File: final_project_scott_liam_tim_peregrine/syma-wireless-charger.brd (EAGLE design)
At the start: 100 x 80 mm, 46 parts, among them U1 SAMD21E

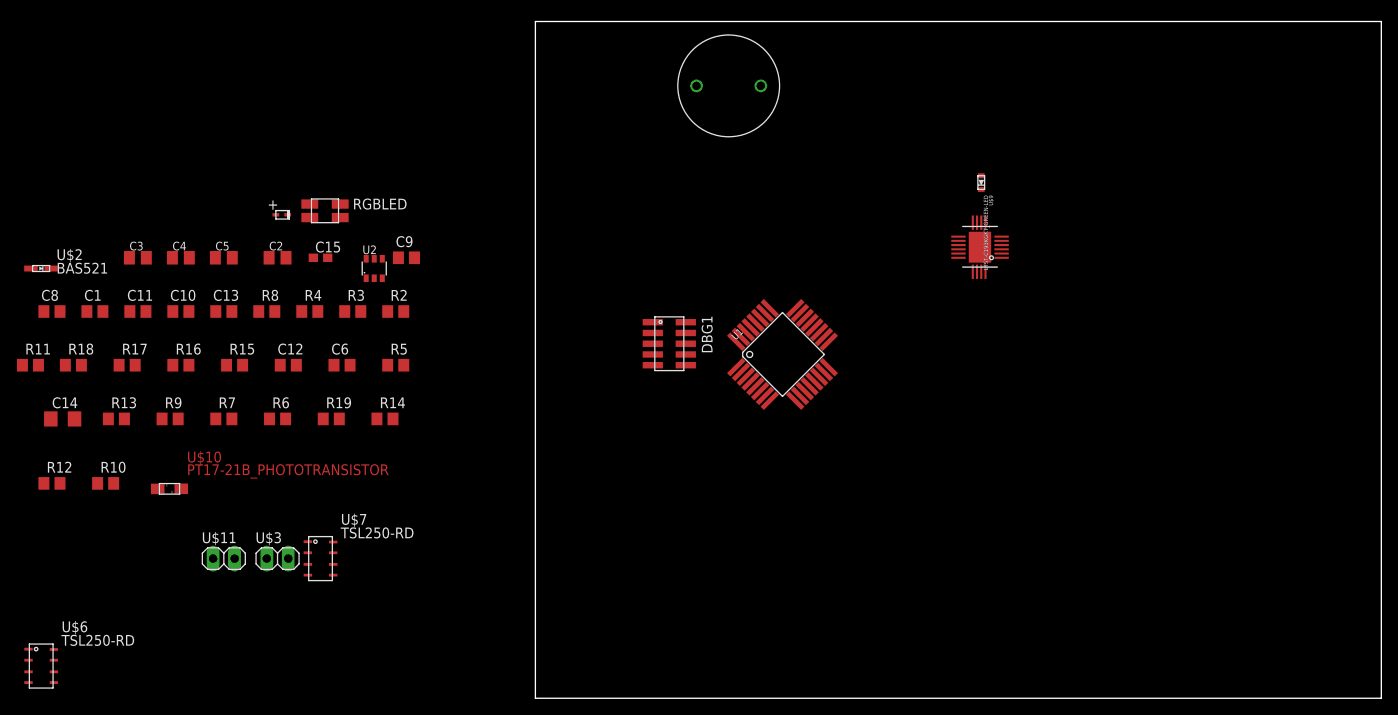
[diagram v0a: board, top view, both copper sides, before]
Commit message: placed parts for transmitter board. no traces yet
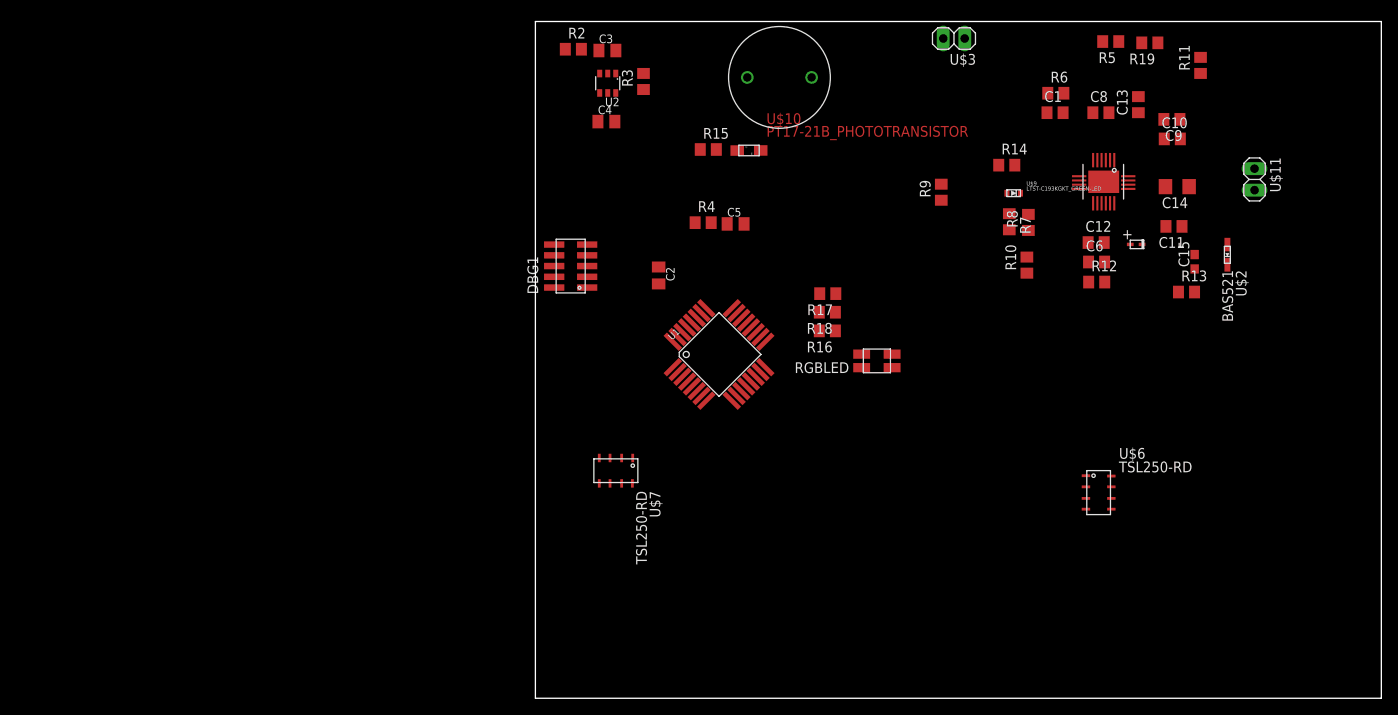
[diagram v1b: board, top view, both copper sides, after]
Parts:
- moved R11 142.8 mm to (78.6, 74.8), turned to 90 degrees
- moved U$2 140.2 mm to (81.8, 52.4), turned to 270 degrees
- moved C14 134.6 mm to (75.9, 60.5), turned to 180 degrees
- moved U$11 129.8 mm to (85.0, 61.3), turned to 270 degrees
- moved R13 127.4 mm to (77.0, 48.0)
- moved U$6 126.7 mm to (66.6, 24.3)
- moved C8 126.2 mm to (66.8, 69.2)
- moved R12 125.8 mm to (66.3, 49.2)
- moved C11 122.9 mm to (75.5, 55.8), turned to 180 degrees
- moved C10 119.0 mm to (75.3, 66.1)
- moved C1 115.9 mm to (61.4, 69.2)
- moved R10 111.9 mm to (58.1, 51.2), turned to 90 degrees
- moved C13 110.8 mm to (71.3, 70.2), turned to 90 degrees
- moved R19 106.5 mm to (72.6, 77.5), turned to 180 degrees
- moved C15 103.3 mm to (77.9, 51.6), turned to 90 degrees
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
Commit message: mostly finished traces
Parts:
- moved U$3 41.5 mm to (8.02, 75.5), turned to 0 degrees
- moved R2 12.6 mm to (5.99, 64.2)
- moved U$7 12.0 mm to (21.5, 26.1), turned to 90 degrees
- moved C4 9.34 mm to (10.9, 59.2)
- moved C8 8.67 mm to (71.8, 76.3), turned to 90 degrees
- moved R3 8.54 mm to (15.8, 64.9)
- moved U2 8.25 mm to (10.6, 64.7)
- moved C3 7.76 mm to (10.5, 69.1)
- moved DBG1 7.63 mm to (8.78, 52.5), turned to 270 degrees
- moved C2 7.16 mm to (17.6, 56.5)
- moved U$5 6.67 mm to (31.6, 71.9)
- moved R9 6.52 mm to (53.5, 56.3)
- moved R19 6.04 mm to (67.1, 75.0)
- moved U$6 5.56 mm to (63.9, 29.2), turned to 180 degrees
- moved U$4 5.00 mm to (45.2, 43.1)
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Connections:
- net GND: now also U$1.GND2
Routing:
- net +5V: track 0.00 -> 156.2 mm, vias 0 -> 4
- net N$20: track 0.00 -> 137.0 mm, vias 0 -> 6
- net VDD: track 0.00 -> 112.2 mm, vias 0 -> 4
- net GND: track 0.00 -> 106.9 mm, vias 0 -> 16
- net ALIGNED: track 0.00 -> 69.0 mm
- net PA17: track 0.00 -> 62.3 mm, vias 0 -> 4
- net RST: track 0.00 -> 46.9 mm
- net N$19: track 0.00 -> 33.5 mm
- net N$7: track 0.00 -> 31.7 mm
- net N$4: track 0.00 -> 26.4 mm, vias 0 -> 2
- net N$9: track 0.00 -> 24.9 mm, vias 0 -> 4
- net ENVSENSE: track 0.00 -> 18.8 mm
- net N$21: track 0.00 -> 15.7 mm
- net SWDCLK-PA30: track 0.00 -> 14.8 mm
- net SWDIO-PA31: track 0.00 -> 14.3 mm, vias 0 -> 2
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- added copper zone on layer 16, net GND
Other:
- board size 100 x 80 mm -> 90.5 x 64.5 mm

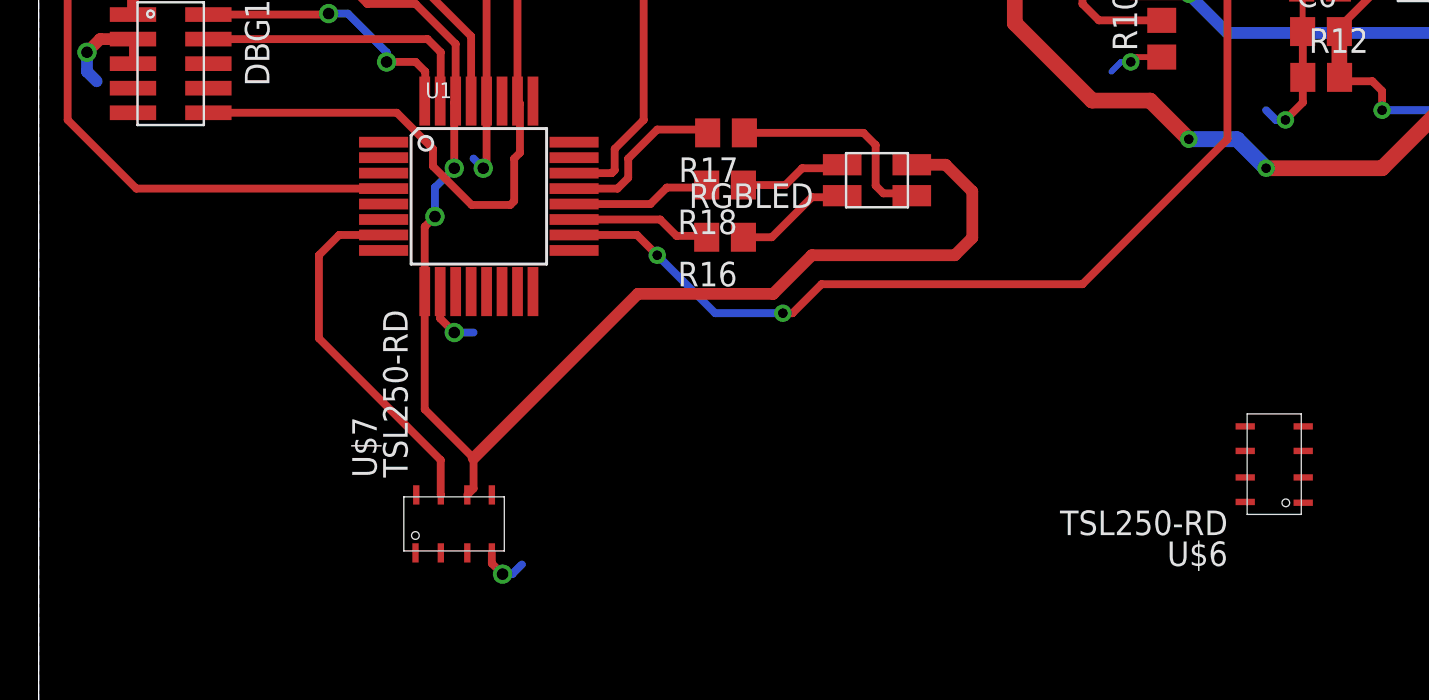
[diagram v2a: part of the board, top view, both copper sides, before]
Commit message: moved the light detectors to be farther from each other
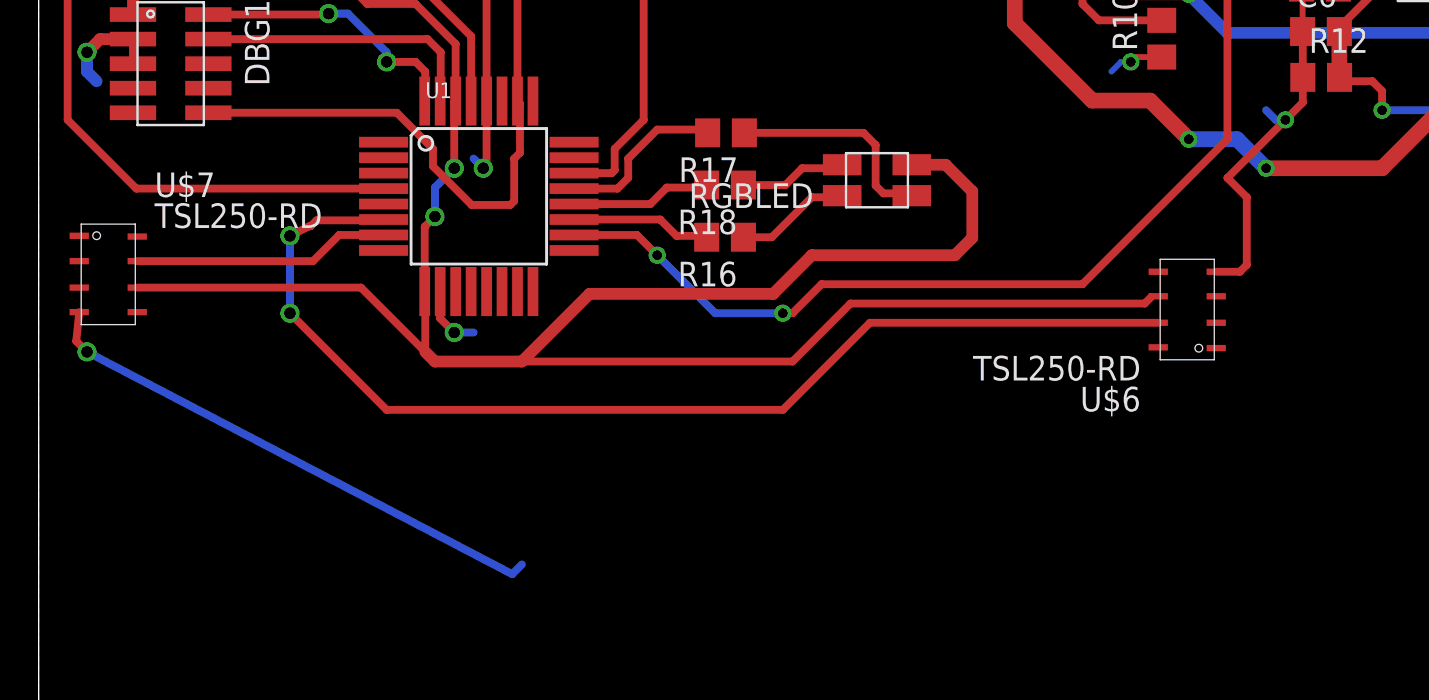
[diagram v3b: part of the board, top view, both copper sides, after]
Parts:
- moved U$7 22.1 mm to (3.60, 39.0), turned to 0 degrees
- moved U$6 9.18 mm to (59.4, 37.2)
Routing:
- net CARSENSE: track 0.00 -> 58.0 mm, vias 0 -> 2
- net VDD: track 112.2 -> 157.8 mm
- net GND: track 106.9 -> 143.0 mm
- net ENVSENSE: track 18.8 -> 13.3 mm
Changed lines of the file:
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@@
 <?xml version="1.0" encoding="utf-8"?>
 <!DOCTYPE eagle SYSTEM "eagle.dtd">
-<eagle version="7.4.0">
+<eagle version="7.5.0">
 <drawing>
 <settings>
@@
 <element name="U$4" library="foe-scale" package="RGBLED" value="RGBLED" x="45.17" y="43.08" rot="R180"/>
 <element name="U$5" library="foe-scale" package="BUZZER" value="BUZZER" x="31.55" y="71.89" rot="R270"/>
-<element name="U$6" library="foe-scale" package="TSL250-RD" value="TSL250-RD" x="63.92" y="29.19" rot="R180"/>
-<element name="U$7" library="foe-scale" package="TSL250-RD" value="TSL250-RD" x="21.49" y="26.1" rot="R90"/>
+<element name="U$6" library="foe-scale" package="TSL250-RD" value="TSL250-RD" x="59.42" y="37.19" rot="R180"/>
+<element name="U$7" library="foe-scale" package="TSL250-RD" value="TSL250-RD" x="3.6" y="39.01"/>
 <element name="U$8" library="foe-scale" package="SOD-523" value="SCHTKYDIODE-523" x="70.52" y="53.65"/>
 <element name="U$9" library="foe-scale" package="LTST-C193KGKT_GREEN-LED" value="LTST-C193KGKT_GREEN-LED" x="56.54" y="59.705"/>
@@
 <via x="21.5" y="36" extent="1-16" drill="0.6"/>
 <wire x1="21.5" y1="36" x2="22.5" y2="36" width="0.4064" layer="16"/>
-<wire x1="23.445" y1="24.6" x2="23.445" y2="24.055" width="0.4064" layer="1"/>
-<wire x1="23.445" y1="24.055" x2="24" y2="23.5" width="0.4064" layer="1"/>
-<via x="24" y="23.5" extent="1-16" drill="0.6"/>
-<wire x1="24" y1="23.5" x2="24.5" y2="23.5" width="0.4064" layer="16"/>
+<wire x1="2.1" y1="37.055" x2="1.945" y2="35.555" width="0.4064" layer="1"/>
+<wire x1="1.945" y1="35.555" x2="2.5" y2="35" width="0.4064" layer="1"/>
+<via x="2.5" y="35" extent="1-16" drill="0.6"/>
+<wire x1="2.5" y1="35" x2="24.5" y2="23.5" width="0.4064" layer="16"/>
 <wire x1="24.5" y1="23.5" x2="25" y2="24" width="0.4064" layer="16"/>
 <wire x1="31.5" y1="71.84" x2="31.55" y2="71.89" width="0.4064" layer="1"/>
@@
 <via x="76" y="51.5" extent="1-16" drill="0.5"/>
 <wire x1="76" y1="51.5" x2="75.5" y2="51" width="0.6096" layer="16"/>
-<wire x1="64.5" y1="47" x2="65.42" y2="31.145" width="0" layer="19" extent="1-1"/>
+<wire x1="60.92" y1="39.145" x2="62.145" y2="39.145" width="0.4064" layer="1"/>
+<wire x1="62.145" y1="39.145" x2="62.5" y2="39.5" width="0.4064" layer="1"/>
+<wire x1="62.5" y1="39.5" x2="62.5" y2="43" width="0.4064" layer="1"/>
+<wire x1="62.5" y1="43" x2="61.5" y2="44" width="0.4064" layer="1"/>
+<wire x1="61.5" y1="44" x2="64.5" y2="47" width="0.4064" layer="1"/>
 </signal>
 <signal name="N$3">
@@
 <wire x1="21.5" y1="44.5" x2="21.5" y2="47.90168125" width="0.4064" layer="1"/>
 <wire x1="21.5" y1="47.90168125" x2="21.572615625" y2="47.974296875" width="0.4064" layer="1"/>
-<wire x1="19.972615625" y1="38.119096875" x2="19.972615625" y2="32.027384375" width="0.4064" layer="1"/>
-<wire x1="19.972615625" y1="32.027384375" x2="22.5" y2="29.5" width="0.4064" layer="1"/>
-<wire x1="22.5" y1="29.5" x2="22.5" y2="27.925" width="0.4064" layer="1"/>
-<wire x1="22.5" y1="27.925" x2="22.175" y2="27.6" width="0.4064" layer="1"/>
 <wire x1="45.17" y1="44.68" x2="46.92" y2="44.68" width="0.6096" layer="1"/>
 <wire x1="46.92" y1="44.68" x2="48.3" y2="43.3" width="0.6096" layer="1"/>
@@
 <wire x1="47.4" y1="40" x2="40" y2="40" width="0.6096" layer="1"/>
 <wire x1="40" y1="40" x2="38" y2="38" width="0.6096" layer="1"/>
-<wire x1="38" y1="38" x2="31" y2="38" width="0.6096" layer="1"/>
-<wire x1="31" y1="38" x2="22.5" y2="29.5" width="0.6096" layer="1"/>
+<wire x1="38" y1="38" x2="28.5" y2="38" width="0.6096" layer="1"/>
+<wire x1="5.1" y1="38.325" x2="16.675" y2="38.325" width="0.4064" layer="1"/>
+<wire x1="16.675" y1="38.325" x2="20" y2="35" width="0.4064" layer="1"/>
+<wire x1="28.5" y1="38" x2="25" y2="34.5" width="0.6096" layer="1"/>
+<wire x1="25" y1="34.5" x2="20.5" y2="34.5" width="0.6096" layer="1"/>
+<wire x1="20.5" y1="34.5" x2="20" y2="35" width="0.6096" layer="1"/>
+<wire x1="20" y1="37" x2="20" y2="35" width="0.4064" layer="1"/>
+<wire x1="20.5" y1="34.5" x2="39" y2="34.5" width="0.4064" layer="1"/>
+<wire x1="39" y1="34.5" x2="42" y2="37.5" width="0.4064" layer="1"/>
+<wire x1="42" y1="37.5" x2="57.21871875" y2="37.5" width="0.4064" layer="1"/>
+<wire x1="57.21871875" y1="37.5" x2="57.550728125" y2="37.832009375" width="0.4064" layer="1"/>
+<wire x1="57.550728125" y1="37.832009375" x2="21.5" y2="44.5" width="0" layer="19" extent="1-16"/>
 </signal>
 <signal name="N$2">
@@
 <contactref element="U$7" pad="OUT"/>
 <wire x1="17.845015625" y1="41.046696875" x2="15.546696875" y2="41.046696875" width="0.4064" layer="1"/>
-<wire x1="15.546696875" y1="41.046696875" x2="14.5" y2="40" width="0.4064" layer="1"/>
-<wire x1="14.5" y1="40" x2="14.5" y2="35.7" width="0.4064" layer="1"/>
-<wire x1="14.5" y1="35.7" x2="20.8" y2="29.4" width="0.4064" layer="1"/>
-<wire x1="20.8" y1="29.4" x2="20.8" y2="27.605" width="0.4064" layer="1"/>
-<wire x1="20.8" y1="27.605" x2="20.805" y2="27.6" width="0.4064" layer="1"/>
+<wire x1="15.546696875" y1="41.046696875" x2="14.195" y2="39.695" width="0.4064" layer="1"/>
+<wire x1="5.1" y1="39.695" x2="14.195" y2="39.695" width="0.4064" layer="1"/>
 </signal>
 <signal name="CARSENSE">
 <contactref element="U1" pad="6"/>
 <contactref element="U$6" pad="OUT"/>
-<wire x1="17.845015625" y1="41.846696875" x2="62.42" y2="28.505" width="0" layer="19" extent="1-1"/>
+<wire x1="57.92" y1="36.505" x2="43.005" y2="36.505" width="0.4064" layer="1"/>
+<wire x1="43.005" y1="36.505" x2="38.5" y2="32" width="0.4064" layer="1"/>
+<wire x1="38.5" y1="32" x2="18" y2="32" width="0.4064" layer="1"/>
+<wire x1="18" y1="32" x2="13" y2="37" width="0.4064" layer="1"/>
+<via x="13" y="37" extent="1-16" drill="0.6" shape="square"/>
+<wire x1="13" y1="37" x2="13" y2="41" width="0.4064" layer="16"/>
+<via x="13" y="41" extent="1-16" drill="0.6" shape="square"/>
+<wire x1="13" y1="41" x2="14" y2="41.5" width="0.4064" layer="1"/>
+<wire x1="14" y1="41.5" x2="14.068759375" y2="41.5" width="0.4064" layer="1"/>
+<wire x1="14.068759375" y1="41.5" x2="14.37279375" y2="41.804034375" width="0.4064" layer="1"/>
+<wire x1="14.37279375" y1="41.804034375" x2="17.802353125" y2="41.804034375" width="0.4064" layer="1"/>
+<wire x1="17.802353125" y1="41.804034375" x2="17.845015625" y2="41.846696875" width="0.4064" layer="1"/>
 </signal>
 <signal name="IMON">
